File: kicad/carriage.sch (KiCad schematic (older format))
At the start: 49 parts, among them CON10 Stepstick_Left_Connector, CON11 Stepstick_Right_Connector, CON12 Stepstick_Left_Connector, CON13 Stepstick_Right_Connector, CON14 Stepstick_Left_Connector, CON15 Stepstick_Right_Connector, CON9 Carriage, Q1 IRLR2905ZPBF, Q2 IRLR2905ZPBF, Q3 FDC6401N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

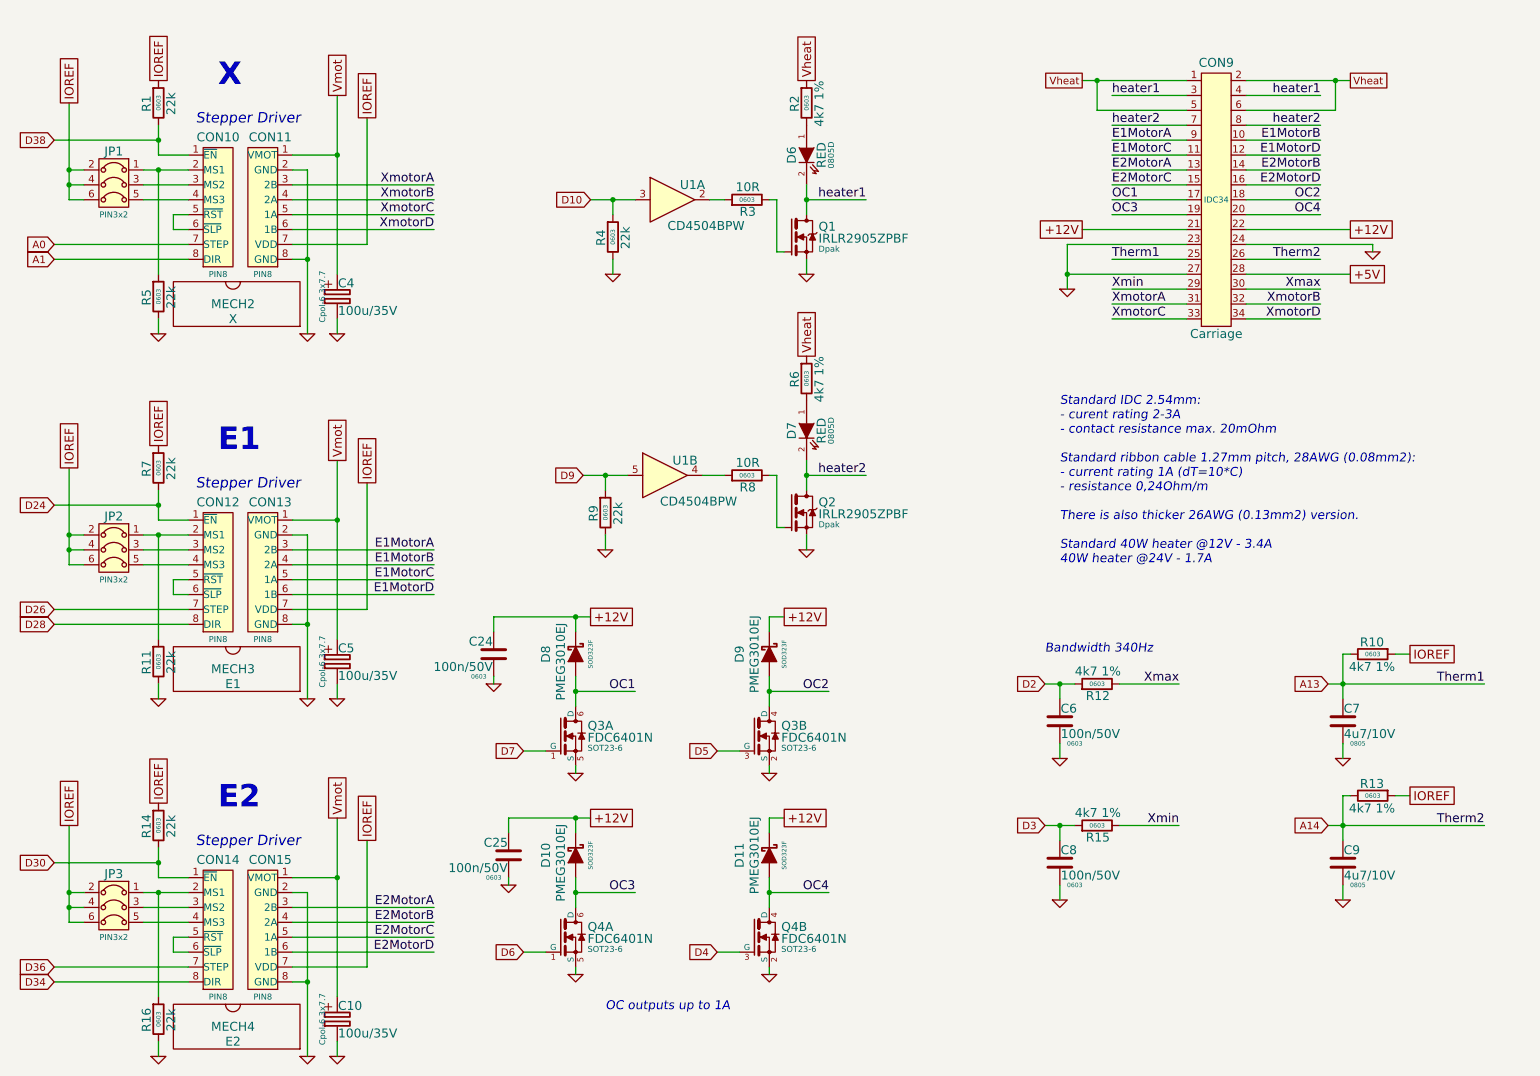
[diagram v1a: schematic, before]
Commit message: Swap pins
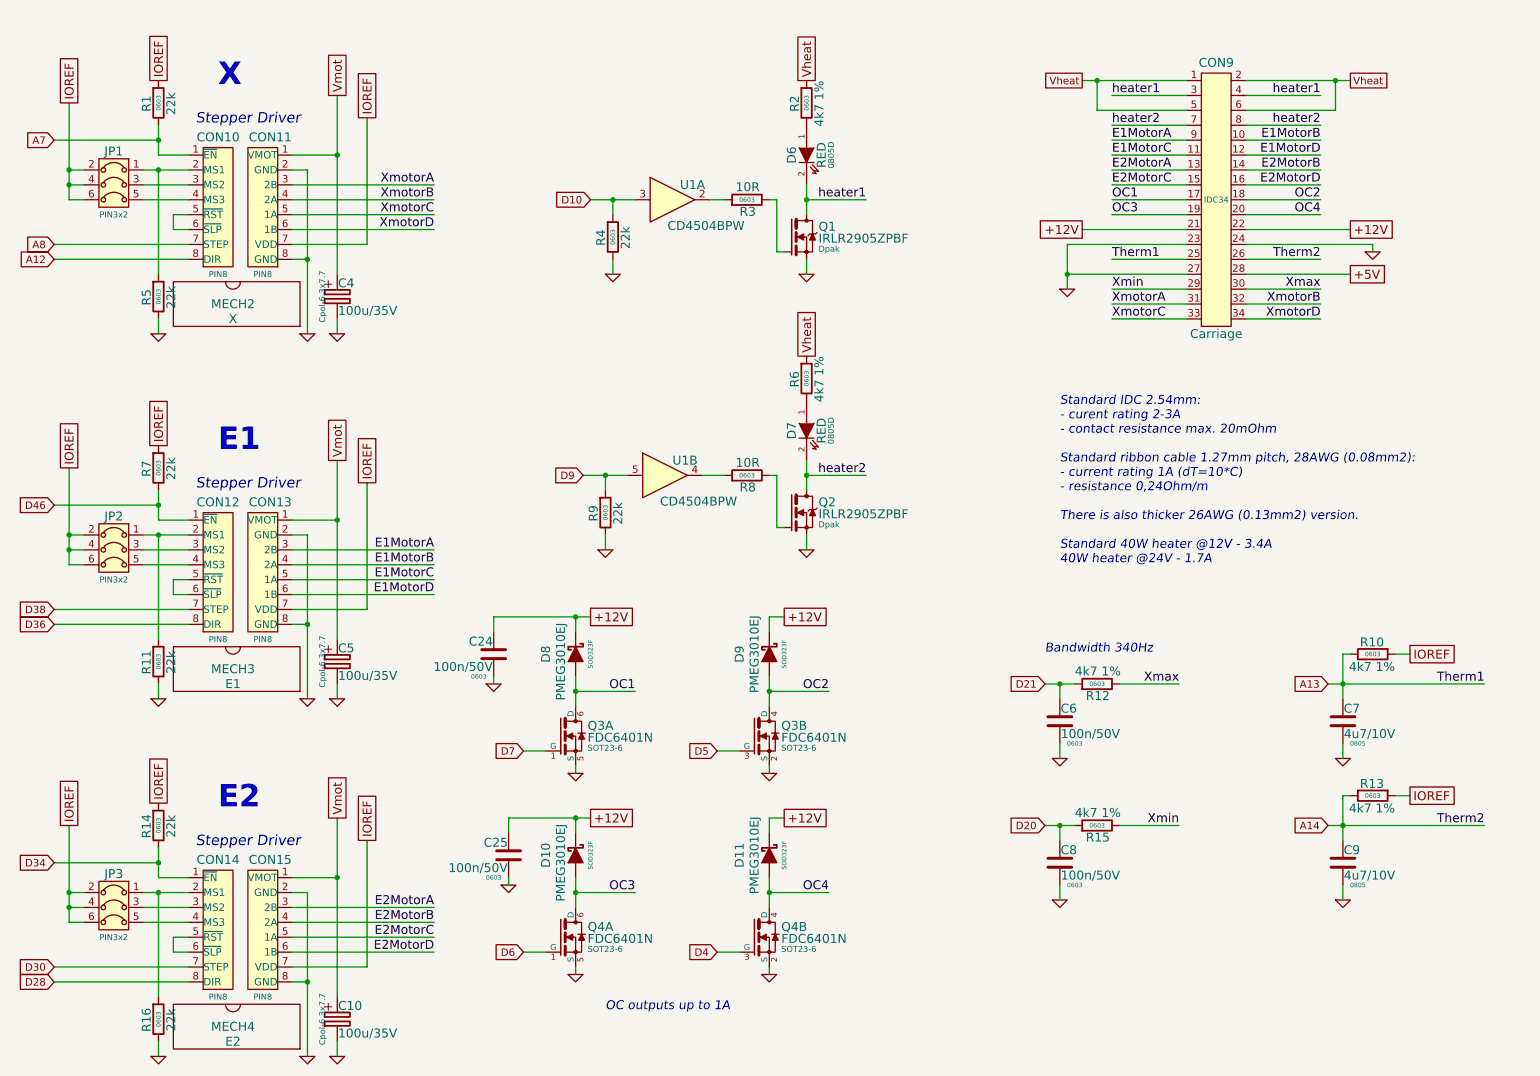
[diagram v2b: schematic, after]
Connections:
- net D26 is gone; now on net D38: CON12.7 (STEP)
- net D28: now also CON14.8 (DIR); no longer CON12.8 (DIR)
- net D30: now also CON14.7 (STEP); no longer CON14.1 (~EN), R14.2
- net D34: now also CON14.1 (~EN), R14.2; no longer CON14.8 (DIR)
- net D36: now also CON12.8 (DIR); no longer CON14.7 (STEP)
- net D38: no longer CON10.1 (~EN), R1.2
- net A0 renamed A8
- net A1 renamed A12
- net D2 renamed D21
- net D24 renamed D46
- net D3 renamed D20
- new net A7: CON10.1 (~EN), R1.2
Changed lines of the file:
@@
 $EndDescr
 Text GLabel 1000 3650 0    50   Input ~ 0
-D24
+D46
 Text GLabel 1000 4350 0    50   Input ~ 0
-D26
+D38
 Text GLabel 1000 4450 0    50   Input ~ 0
+D36
+Text GLabel 1000 1200 0    50   Input ~ 0
+A7
+Text GLabel 1000 1900 0    50   Input ~ 0
+A8
+Text GLabel 1000 2000 0    50   Input ~ 0
+A12
+Text GLabel 1000 6050 0    50   Input ~ 0
+D34
+Text GLabel 1000 6750 0    50   Input ~ 0
+D30
+Text GLabel 1000 6850 0    50   Input ~ 0
 D28
-Text GLabel 1000 1200 0    50   Input ~ 0
-D38
-Text GLabel 1000 1900 0    50   Input ~ 0
-A0
-Text GLabel 1000 2000 0    50   Input ~ 0
-A1
-Text GLabel 1000 6050 0    50   Input ~ 0
-D30
-Text GLabel 1000 6750 0    50   Input ~ 0
-D36
-Text GLabel 1000 6850 0    50   Input ~ 0
-D34
 $Comp
 L GND #PWR04
@@
 $EndComp
 Text GLabel 7650 4850 0    50   Input ~ 0
-D2
+D21
 Text GLabel 7650 5800 0    50   Input ~ 0
-D3
+D20
 $Comp
 L GND #PWR011

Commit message: Route
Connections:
- net D28: now also CON12.1 (~EN), R7.2; no longer CON14.8 (DIR)
- net D30: now also CON12.7 (STEP); no longer CON14.7 (STEP)
- net D34: now also CON12.8 (DIR); no longer CON14.1 (~EN), R14.2
- net D36: now also CON14.1 (~EN), R14.2; no longer CON12.8 (DIR)
- net D38: now also CON14.7 (STEP); no longer CON12.7 (STEP)
- net D46: now also CON14.8 (DIR); no longer CON12.1 (~EN), R7.2
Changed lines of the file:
@@
 $EndDescr
 Text GLabel 1000 3650 0    50   Input ~ 0
-D46
+D28
 Text GLabel 1000 4350 0    50   Input ~ 0
-D38
+D30
 Text GLabel 1000 4450 0    50   Input ~ 0
-D36
+D34
 Text GLabel 1000 1200 0    50   Input ~ 0
 A7
@@
 A12
 Text GLabel 1000 6050 0    50   Input ~ 0
-D34
+D36
 Text GLabel 1000 6750 0    50   Input ~ 0
-D30
+D38
 Text GLabel 1000 6850 0    50   Input ~ 0
-D28
+D46
 $Comp
 L GND #PWR04

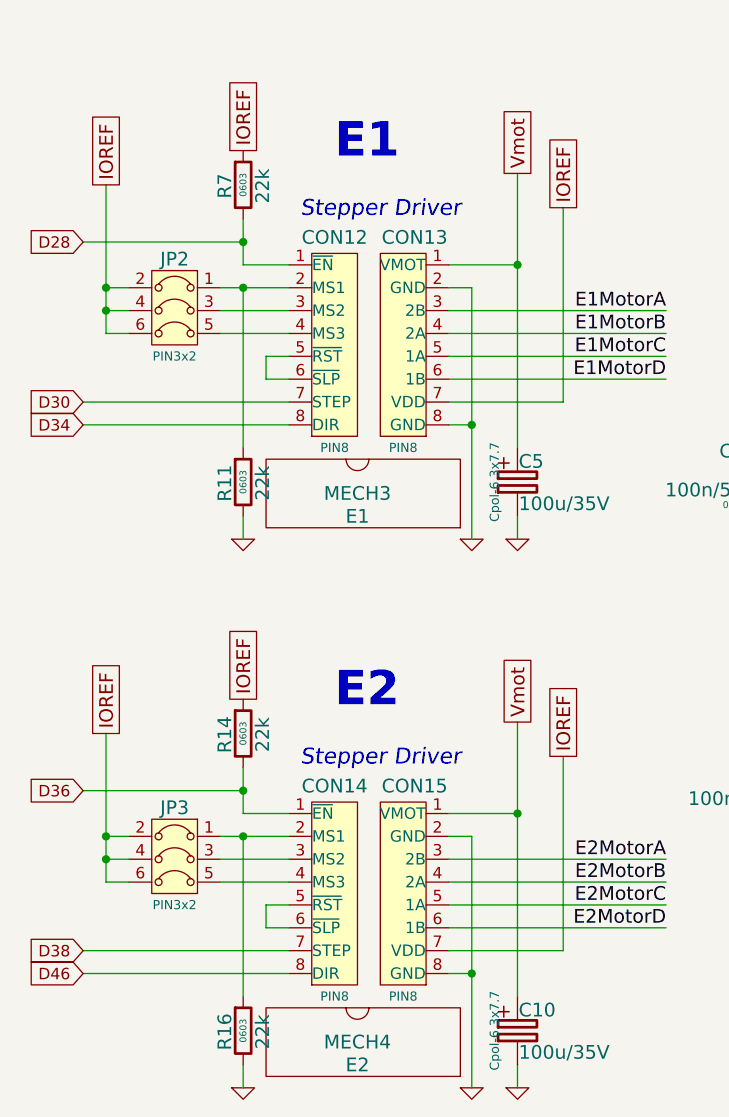
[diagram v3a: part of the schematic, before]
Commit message: Exchange stepstick connections.
Simplify layout
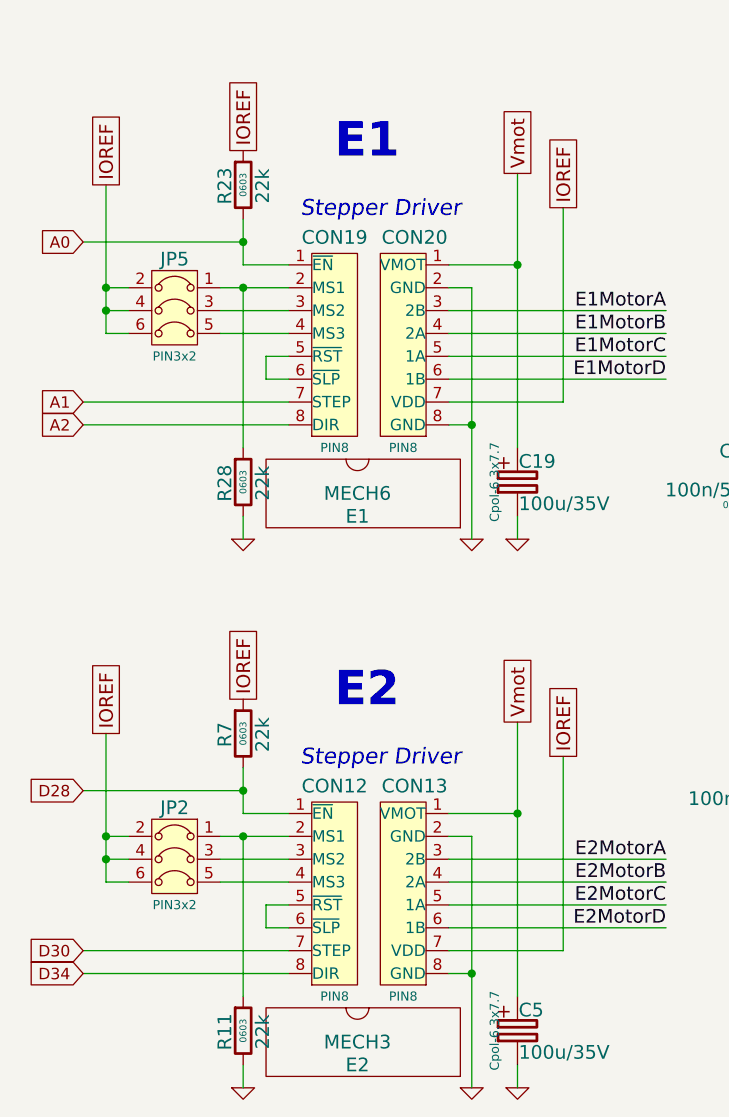
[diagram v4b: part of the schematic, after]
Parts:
- removed C10: 100u/35V, Cpol-6.3x7.7, symbol Cpol
- removed CON14: Stepstick_Left_Connector, PIN8, symbol Stepstick_Left_Connector
- removed CON15: Stepstick_Right_Connector, PIN8, symbol Stepstick_Right_Connector
- removed JP3: Jumper3, PIN3x2, symbol Jumper3
- removed MECH4: E2, symbol stepstickFootprint
- removed R14, R16: 22k, 0603, symbol R
- added C19: 100u/35V, Cpol-6.3x7.7, symbol Cpol
- added CON19: Stepstick_Left_Connector, PIN8, symbol Stepstick_Left_Connector
- added CON20: Stepstick_Right_Connector, PIN8, symbol Stepstick_Right_Connector
- added JP5: Jumper3, PIN3x2, symbol Jumper3
- added MECH6: E1, symbol stepstickFootprint
- added R23, R28: 22k, 0603, symbol R
- MECH3: value E1 -> E2
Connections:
- net E1MotorA: now also CON20.3 (2B); no longer CON13.3 (2B)
- net E1MotorB: now also CON20.4 (2A); no longer CON13.4 (2A)
- net E1MotorC: now also CON20.5 (1A); no longer CON13.5 (1A)
- net E1MotorD: now also CON20.6 (1B); no longer CON13.6 (1B)
- net E2MotorA: now also CON13.3 (2B)
- net E2MotorB: now also CON13.4 (2A)
- net E2MotorC: now also CON13.5 (1A)
- net E2MotorD: now also CON13.6 (1B)
- net GND: now also C19.2, CON20.2 (GND), CON20.8 (GND), R28.2
- net IOREF: now also CON20.7 (VDD), JP5.2, JP5.4, JP5.6, R23.1
- net Vmot: now also C19.1, CON20.1 (VMOT)
- new net: CON19.2 (MS1), JP5.1, R28.1
- new net: CON19.3 (MS2), JP5.3
- new net: CON19.4 (MS3), JP5.5
- new net: CON19.5 (~RST), CON19.6 (~SLP)
- new net A0: CON19.1 (~EN), R23.2
- new net A1: CON19.7 (STEP)
- new net A2: CON19.8 (DIR)
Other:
- moved on the sheet: C5, CON12, CON13, JP2, MECH3, R11, R7

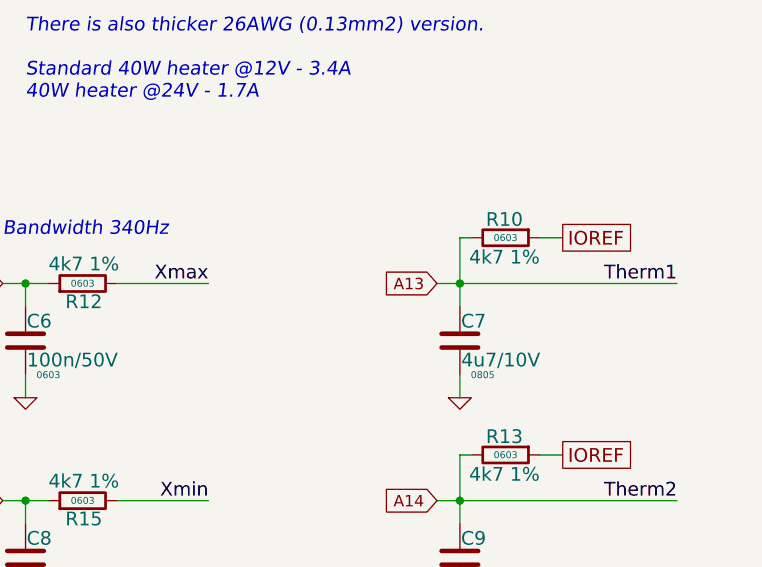
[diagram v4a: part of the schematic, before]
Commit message: Pin swap. Route.
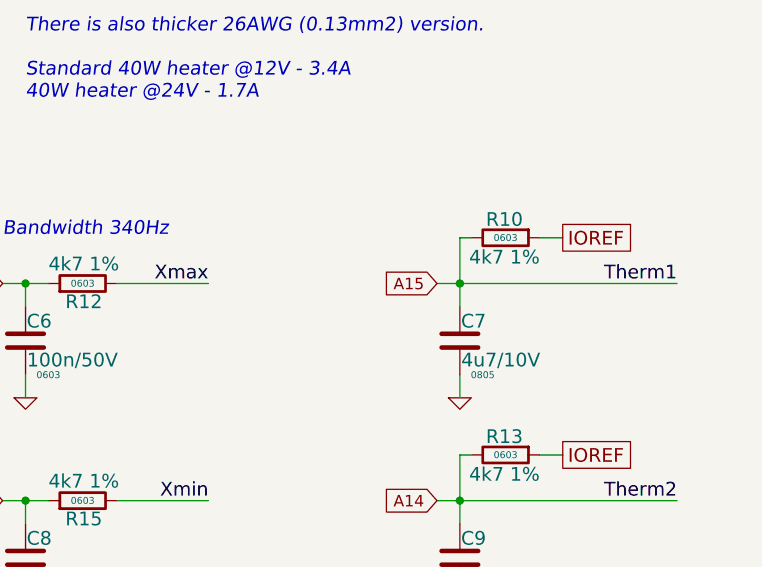
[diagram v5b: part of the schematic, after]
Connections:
- net A13 renamed A15
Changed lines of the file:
@@
 $EndComp
 Text GLabel 9550 4850 0    50   Input ~ 0
-A13
+A15
 $Comp
 L GND #PWR08
